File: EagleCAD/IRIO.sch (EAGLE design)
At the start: 17 parts, among them Q2 MOSFET-PCHANNEL, Q3 MOSFET-NCHANNEL

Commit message: Add files via upload
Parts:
- removed C2: (no value), SparkFun-Capacitors:CAP0805
- removed Q2: MOSFET-PCHANNEL, SparkFun-DiscreteSemi:MOSFET-PCHANNEL
- removed R3, R5: 10K, SparkFun-Passives:RESISTOR0805-RES
- removed R4: 3K09, SparkFun-Passives:RESISTOR0805-RES
- removed U$5, U$6: SMD-PAD1SMD-PAD80X32, CuriousTech:SMD-PAD1SMD-PAD80X32
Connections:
- removed net BATT: Q2.S, R5.2, U$5.P$1
- removed net IO8: R3.1, R4.2, U$6.P$1
- removed net N$5: Q2.D, R3.2
- removed net N$7: C2.2, Q2.G, R5.1
- net GND: no longer R4.1
- net RX: no longer C2.1
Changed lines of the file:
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@@
 <part name="U$4" library="CuriousTech" deviceset="SMD-PAD1" device="SMD-PAD80X32"/>
 <part name="RC" library="SparkFun-Sensors" deviceset="BRM-2A18" device="RA" value="TSSOPxx38"/>
-<part name="R3" library="SparkFun-Passives" deviceset="RESISTOR" device="0805-RES" value="10K"/>
-<part name="R4" library="SparkFun-Passives" deviceset="RESISTOR" device="0805-RES" value="3K09"/>
-<part name="GND1" library="supply1" deviceset="GND" device=""/>
-<part name="U$5" library="CuriousTech" deviceset="SMD-PAD1" device="SMD-PAD80X32"/>
-<part name="U$6" library="CuriousTech" deviceset="SMD-PAD1" device="SMD-PAD80X32"/>
-<part name="Q2" library="SparkFun-DiscreteSemi" deviceset="MOSFET-PCHANNEL" device=""/>
-<part name="R5" library="SparkFun-Passives" deviceset="RESISTOR" device="0805-RES" value="10K"/>
-<part name="C2" library="SparkFun-Capacitors" deviceset="CAP" device="0805"/>
 <part name="Q3" library="SparkFun-DiscreteSemi" deviceset="MOSFET-NCHANNEL" device="AO3404A" value="MOSFET-NCHANNEL"/>
 <part name="LED1" library="led" library_urn="urn:adsk.eagle:library:259" deviceset="LED" device="5MM" package3d_urn="urn:adsk.eagle:package:15799/2"/>
@@
 <attribute name="NAME" x="15.24" y="94.742" size="1.778" layer="95"/>
 <attribute name="VALUE" x="15.24" y="81.28" size="1.778" layer="96"/>
-</instance>
-<instance part="R3" gate="G$1" x="127" y="86.36" smashed="yes" rot="R90">
-<attribute name="NAME" x="125.5014" y="82.55" size="1.778" layer="95" rot="R90"/>
-<attribute name="VALUE" x="130.302" y="82.55" size="1.778" layer="96" rot="R90"/>
-</instance>
-<instance part="R4" gate="G$1" x="127" y="66.04" smashed="yes" rot="R90">
-<attribute name="NAME" x="125.5014" y="62.23" size="1.778" layer="95" rot="R90"/>
-<attribute name="VALUE" x="130.302" y="62.23" size="1.778" layer="96" rot="R90"/>
-</instance>
-<instance part="GND1" gate="1" x="127" y="53.34" smashed="yes">
-<attribute name="VALUE" x="124.46" y="50.8" size="1.778" layer="96"/>
-</instance>
-<instance part="U$5" gate="G$1" x="139.7" y="119.38" smashed="yes"/>
-<instance part="U$6" gate="G$1" x="142.24" y="76.2" smashed="yes"/>
-<instance part="Q2" gate="G$1" x="127" y="101.6" smashed="yes" rot="MR180">
-<attribute name="NAME" x="132.08" y="99.06" size="1.778" layer="95" rot="MR180"/>
-<attribute name="VALUE" x="132.08" y="101.6" size="1.778" layer="96" rot="MR180"/>
-</instance>
-<instance part="R5" gate="G$1" x="111.76" y="111.76" smashed="yes" rot="R90">
-<attribute name="NAME" x="110.2614" y="107.95" size="1.778" layer="95" rot="R90"/>
-<attribute name="VALUE" x="115.062" y="107.95" size="1.778" layer="96" rot="R90"/>
-</instance>
-<instance part="C2" gate="G$1" x="104.14" y="101.6" smashed="yes" rot="R90">
-<attribute name="NAME" x="101.219" y="103.124" size="1.778" layer="95" rot="R90"/>
-<attribute name="VALUE" x="106.299" y="103.124" size="1.778" layer="96" rot="R90"/>
 </instance>
 <instance part="Q3" gate="G$1" x="73.66" y="68.58" smashed="yes">
@@
 <wire x1="30.48" y1="88.9" x2="38.1" y2="88.9" width="0.1524" layer="91"/>
 <label x="38.1" y="88.9" size="1.778" layer="95" xref="yes"/>
-</segment>
-<segment>
-<pinref part="GND1" gate="1" pin="GND"/>
-<pinref part="R4" gate="G$1" pin="1"/>
-<wire x1="127" y1="55.88" x2="127" y2="60.96" width="0.1524" layer="91"/>
 </segment>
 <segment>
@@
 <label x="53.34" y="68.58" size="1.778" layer="95" rot="R180" xref="yes"/>
 </segment>
-<segment>
-<pinref part="C2" gate="G$1" pin="1"/>
-<wire x1="99.06" y1="101.6" x2="93.98" y2="101.6" width="0.1524" layer="91"/>
-<label x="93.98" y="101.6" size="1.778" layer="95" rot="R180" xref="yes"/>
-</segment>
 </net>
 <net name="TX" class="0">
@@
 </segment>
 </net>
-<net name="IO8" class="0">
-<segment>
-<pinref part="R4" gate="G$1" pin="2"/>
-<pinref part="R3" gate="G$1" pin="1"/>
-<wire x1="127" y1="71.12" x2="127" y2="76.2" width="0.1524" layer="91"/>
-<pinref part="U$6" gate="G$1" pin="P$1"/>
-<wire x1="127" y1="76.2" x2="127" y2="81.28" width="0.1524" layer="91"/>
-<wire x1="137.16" y1="76.2" x2="127" y2="76.2" width="0.1524" layer="91"/>
-<junction x="127" y="76.2"/>
-<label x="132.08" y="76.2" size="1.778" layer="95" rot="R270" xref="yes"/>
-</segment>
-</net>
-<net name="N$5" class="0">
-<segment>
-<pinref part="R3" gate="G$1" pin="2"/>
-<pinref part="Q2" gate="G$1" pin="D"/>
-<wire x1="127" y1="91.44" x2="127" y2="96.52" width="0.1524" layer="91"/>
-</segment>
-</net>
-<net name="BATT" class="0">
-<segment>
-<pinref part="Q2" gate="G$1" pin="S"/>
-<pinref part="U$5" gate="G$1" pin="P$1"/>
-<wire x1="127" y1="106.68" x2="127" y2="119.38" width="0.1524" layer="91"/>
-<wire x1="127" y1="119.38" x2="134.62" y2="119.38" width="0.1524" layer="91"/>
-<wire x1="127" y1="119.38" x2="111.76" y2="119.38" width="0.1524" layer="91"/>
-<junction x="127" y="119.38"/>
-<pinref part="R5" gate="G$1" pin="2"/>
-<wire x1="111.76" y1="119.38" x2="111.76" y2="116.84" width="0.1524" layer="91"/>
-<label x="132.08" y="119.38" size="1.778" layer="95" rot="R90" xref="yes"/>
-</segment>
-</net>
-<net name="N$7" class="0">
-<segment>
-<pinref part="Q2" gate="G$1" pin="G"/>
-<wire x1="119.38" y1="101.6" x2="111.76" y2="101.6" width="0.1524" layer="91"/>
-<pinref part="R5" gate="G$1" pin="1"/>
-<wire x1="111.76" y1="101.6" x2="106.68" y2="101.6" width="0.1524" layer="91"/>
-<wire x1="111.76" y1="106.68" x2="111.76" y2="101.6" width="0.1524" layer="91"/>
-<junction x="111.76" y="101.6"/>
-<pinref part="C2" gate="G$1" pin="2"/>
-</segment>
-</net>

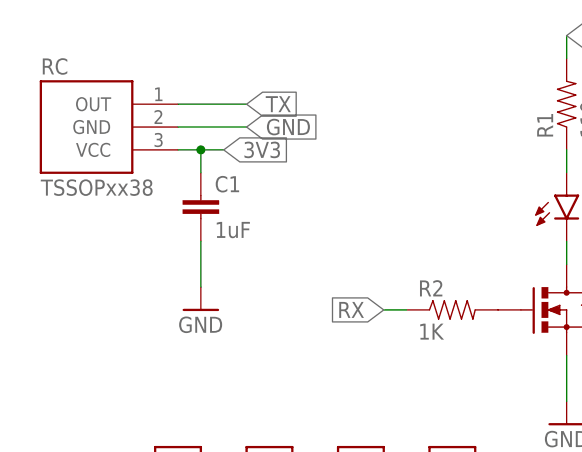
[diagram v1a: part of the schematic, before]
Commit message: Slimmer design with  TSOP39438
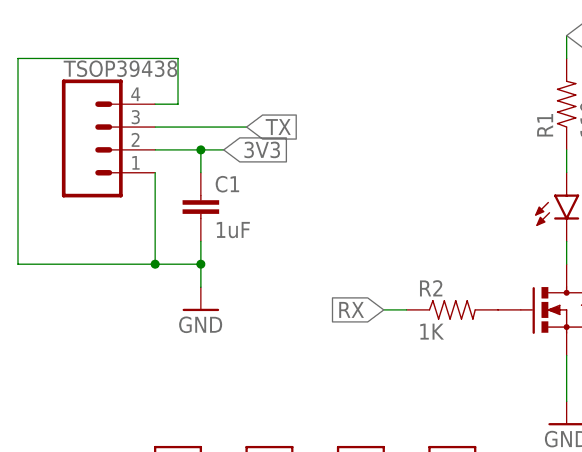
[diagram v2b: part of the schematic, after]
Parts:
- removed RC: TSSOPxx38, SparkFun-Sensors:BRM-2A18RA
- added TSOP39438: (no value), SparkFun-Connectors:CONN_041X04_NO_SILK
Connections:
- net 3V3: now also TSOP39438.2; no longer RC.VCC
- net GND: now also TSOP39438.1, TSOP39438.4; no longer RC.GND
- net TX: now also TSOP39438.3; no longer RC.OUT
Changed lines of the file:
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@@
 <layer number="230" name="230bmp" color="7" fill="1" visible="yes" active="yes"/>
 <layer number="231" name="231bmp" color="7" fill="1" visible="yes" active="yes"/>
+<layer number="232" name="Eagle3D_PG2" color="7" fill="1" visible="yes" active="yes"/>
+<layer number="233" name="Eagle3D_PG3" color="7" fill="1" visible="yes" active="yes"/>
 <layer number="248" name="Housing" color="7" fill="1" visible="yes" active="yes"/>
 <layer number="249" name="Edge" color="7" fill="1" visible="yes" active="yes"/>
@@
 <part name="U$1" library="CuriousTech" deviceset="SMD-PAD1" device="SMD-PAD80X32"/>
 <part name="U$4" library="CuriousTech" deviceset="SMD-PAD1" device="SMD-PAD80X32"/>
-<part name="RC" library="SparkFun-Sensors" deviceset="BRM-2A18" device="RA" value="TSSOPxx38"/>
 <part name="Q3" library="SparkFun-DiscreteSemi" deviceset="MOSFET-NCHANNEL" device="AO3404A" value="MOSFET-NCHANNEL"/>
 <part name="LED1" library="led" library_urn="urn:adsk.eagle:library:259" deviceset="LED" device="5MM" package3d_urn="urn:adsk.eagle:package:15799/2"/>
 <part name="C1" library="SparkFun-Capacitors" deviceset="CAP" device="0805" value="1uF"/>
 <part name="GND2" library="supply1" deviceset="GND" device=""/>
+<part name="TSOP39438" library="SparkFun-Connectors" library_urn="urn:adsk.eagle:library:513" deviceset="CONN_04" device="1X04_NO_SILK" package3d_urn="urn:adsk.eagle:package:38094/1"/>
 </parts>
 <sheets>
@@
 <instance part="U$1" gate="G$1" x="50.8" y="48.26" smashed="yes" rot="R90"/>
 <instance part="U$4" gate="G$1" x="60.96" y="48.26" smashed="yes" rot="R90"/>
-<instance part="RC" gate="G$1" x="20.32" y="88.9" smashed="yes">
-<attribute name="NAME" x="15.24" y="94.742" size="1.778" layer="95"/>
-<attribute name="VALUE" x="15.24" y="81.28" size="1.778" layer="96"/>
-</instance>
 <instance part="Q3" gate="G$1" x="73.66" y="68.58" smashed="yes">
 <attribute name="NAME" x="78.74" y="71.12" size="1.778" layer="95"/>
@@
 <instance part="GND2" gate="1" x="33.02" y="68.58" smashed="yes">
 <attribute name="VALUE" x="30.48" y="66.04" size="1.778" layer="96"/>
+</instance>
+<instance part="TSOP39438" gate="G$1" x="22.86" y="86.36" smashed="yes">
+<attribute name="VALUE" x="17.78" y="78.994" size="1.778" layer="96" font="vector"/>
+<attribute name="NAME" x="17.78" y="94.488" size="1.778" layer="95" font="vector"/>
 </instance>
 </instances>
@@
 </segment>
 <segment>
-<pinref part="RC" gate="G$1" pin="GND"/>
-<wire x1="30.48" y1="88.9" x2="38.1" y2="88.9" width="0.1524" layer="91"/>
-<label x="38.1" y="88.9" size="1.778" layer="95" xref="yes"/>
-</segment>
-<segment>
 <pinref part="C1" gate="G$1" pin="2"/>
-<wire x1="33.02" y1="76.2" x2="33.02" y2="71.12" width="0.1524" layer="91"/>
+<wire x1="33.02" y1="76.2" x2="33.02" y2="73.66" width="0.1524" layer="91"/>
 <pinref part="GND2" gate="1" pin="GND"/>
+<pinref part="TSOP39438" gate="G$1" pin="1"/>
+<wire x1="33.02" y1="73.66" x2="33.02" y2="71.12" width="0.1524" layer="91"/>
+<wire x1="33.02" y1="73.66" x2="27.94" y2="73.66" width="0.1524" layer="91"/>
+<wire x1="27.94" y1="73.66" x2="27.94" y2="83.82" width="0.1524" layer="91"/>
+<junction x="33.02" y="73.66"/>
+<pinref part="TSOP39438" gate="G$1" pin="4"/>
+<wire x1="27.94" y1="91.44" x2="30.48" y2="91.44" width="0.1524" layer="91"/>
+<wire x1="30.48" y1="91.44" x2="30.48" y2="96.52" width="0.1524" layer="91"/>
+<wire x1="30.48" y1="96.52" x2="12.7" y2="96.52" width="0.1524" layer="91"/>
+<wire x1="12.7" y1="96.52" x2="12.7" y2="73.66" width="0.1524" layer="91"/>
+<wire x1="12.7" y1="73.66" x2="27.94" y2="73.66" width="0.1524" layer="91"/>
+<junction x="27.94" y="73.66"/>
 </segment>
 </net>
@@
 </segment>
 <segment>
-<pinref part="RC" gate="G$1" pin="VCC"/>
-<wire x1="30.48" y1="86.36" x2="33.02" y2="86.36" width="0.1524" layer="91"/>
 <label x="35.56" y="86.36" size="1.778" layer="95" xref="yes"/>
 <pinref part="C1" gate="G$1" pin="1"/>
@@
 <wire x1="33.02" y1="83.82" x2="33.02" y2="86.36" width="0.1524" layer="91"/>
 <junction x="33.02" y="86.36"/>
+<pinref part="TSOP39438" gate="G$1" pin="2"/>
+<wire x1="27.94" y1="86.36" x2="33.02" y2="86.36" width="0.1524" layer="91"/>
 </segment>
 <segment>
@@
 </segment>
 <segment>
-<pinref part="RC" gate="G$1" pin="OUT"/>
-<wire x1="30.48" y1="91.44" x2="38.1" y2="91.44" width="0.1524" layer="91"/>
-<label x="38.1" y="91.44" size="1.778" layer="95" xref="yes"/>
+<wire x1="27.94" y1="88.9" x2="38.1" y2="88.9" width="0.1524" layer="91"/>
+<label x="38.1" y="88.9" size="1.778" layer="95" xref="yes"/>
+<pinref part="TSOP39438" gate="G$1" pin="3"/>
 </segment>
 </net>

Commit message: Corrected footprint for TSOP39438
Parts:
- TSOP39438: device SparkFun-Connectors:CONN_041X04_NO_SILK -> SparkFun-Connectors:CONN_041.27MM
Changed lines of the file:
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@@
 <part name="C1" library="SparkFun-Capacitors" deviceset="CAP" device="0805" value="1uF"/>
 <part name="GND2" library="supply1" deviceset="GND" device=""/>
-<part name="TSOP39438" library="SparkFun-Connectors" library_urn="urn:adsk.eagle:library:513" deviceset="CONN_04" device="1X04_NO_SILK" package3d_urn="urn:adsk.eagle:package:38094/1"/>
+<part name="TSOP39438" library="SparkFun-Connectors" library_urn="urn:adsk.eagle:library:513" deviceset="CONN_04" device="1.27MM" package3d_urn="urn:adsk.eagle:package:38086/1"/>
 </parts>
 <sheets>
@@
 <wire x1="33.02" y1="76.2" x2="33.02" y2="73.66" width="0.1524" layer="91"/>
 <pinref part="GND2" gate="1" pin="GND"/>
-<pinref part="TSOP39438" gate="G$1" pin="1"/>
 <wire x1="33.02" y1="73.66" x2="33.02" y2="71.12" width="0.1524" layer="91"/>
 <wire x1="33.02" y1="73.66" x2="27.94" y2="73.66" width="0.1524" layer="91"/>
 <wire x1="27.94" y1="73.66" x2="27.94" y2="83.82" width="0.1524" layer="91"/>
 <junction x="33.02" y="73.66"/>
-<pinref part="TSOP39438" gate="G$1" pin="4"/>
 <wire x1="27.94" y1="91.44" x2="30.48" y2="91.44" width="0.1524" layer="91"/>
 <wire x1="30.48" y1="91.44" x2="30.48" y2="96.52" width="0.1524" layer="91"/>
@@
 <wire x1="12.7" y1="73.66" x2="27.94" y2="73.66" width="0.1524" layer="91"/>
 <junction x="27.94" y="73.66"/>
+<pinref part="TSOP39438" gate="G$1" pin="1"/>
+<pinref part="TSOP39438" gate="G$1" pin="4"/>
 </segment>
 </net>
@@
 <wire x1="33.02" y1="83.82" x2="33.02" y2="86.36" width="0.1524" layer="91"/>
 <junction x="33.02" y="86.36"/>
+<wire x1="27.94" y1="86.36" x2="33.02" y2="86.36" width="0.1524" layer="91"/>
 <pinref part="TSOP39438" gate="G$1" pin="2"/>
-<wire x1="27.94" y1="86.36" x2="33.02" y2="86.36" width="0.1524" layer="91"/>
 </segment>
 <segment>
